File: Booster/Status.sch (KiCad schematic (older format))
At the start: 32 parts

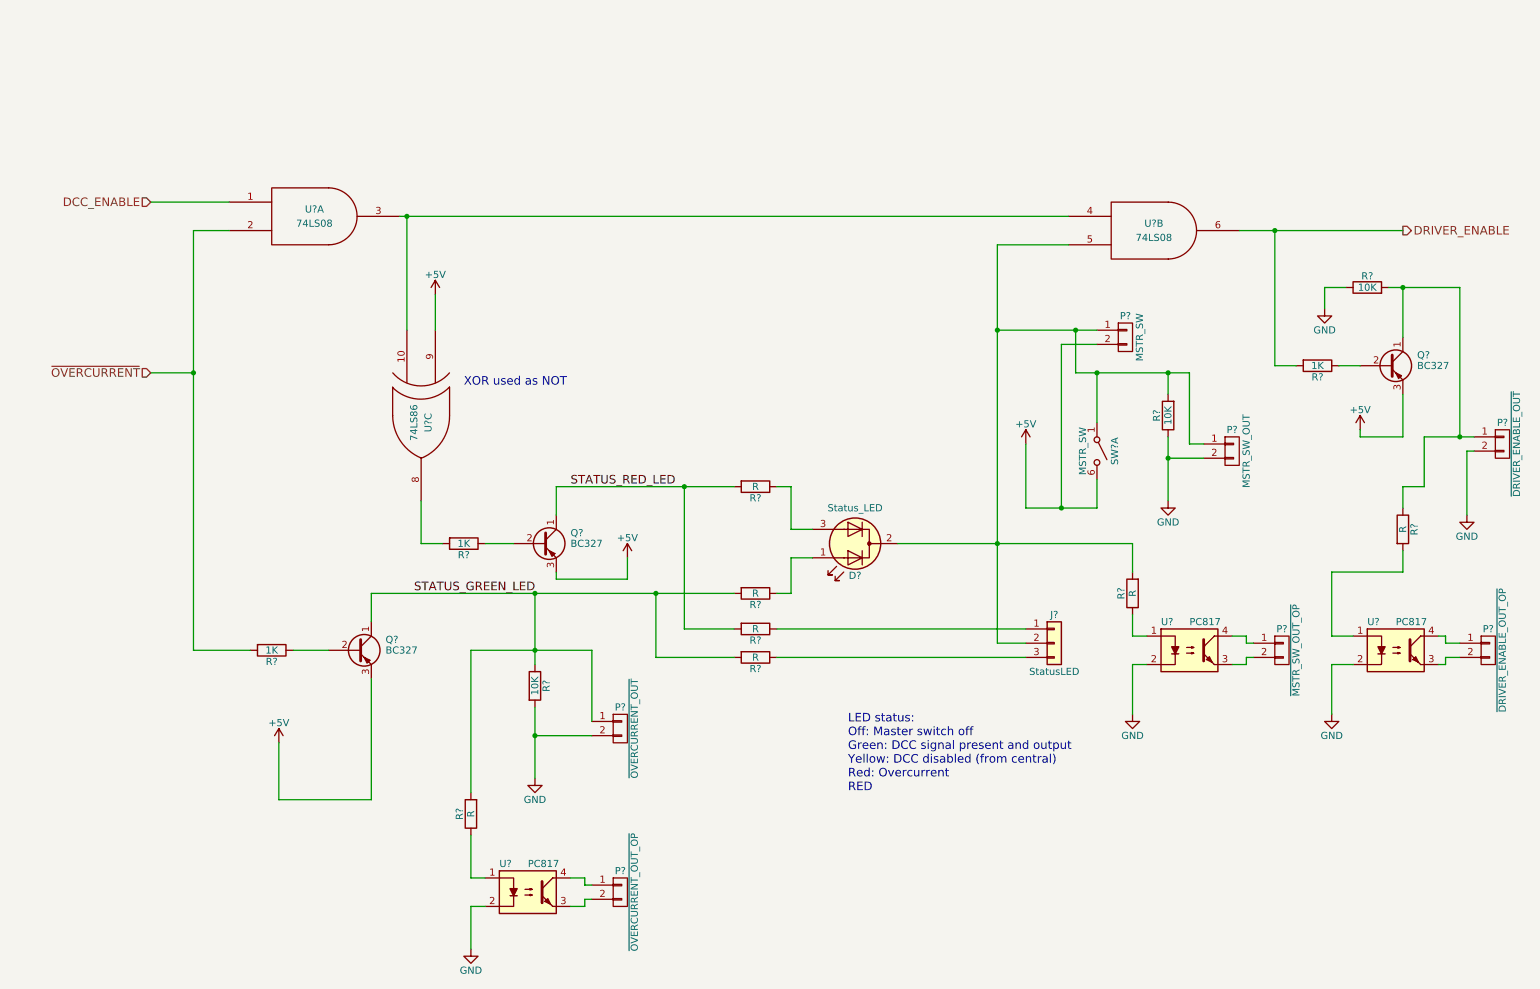
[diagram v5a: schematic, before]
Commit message: Added DCC Enable inverter. Primarely to allow meassuring track voltage easily - by enabling output with no DCC signal giving a steady 12V on the track. Replaced AND gates with NAND to free up the necessary XOR gate.
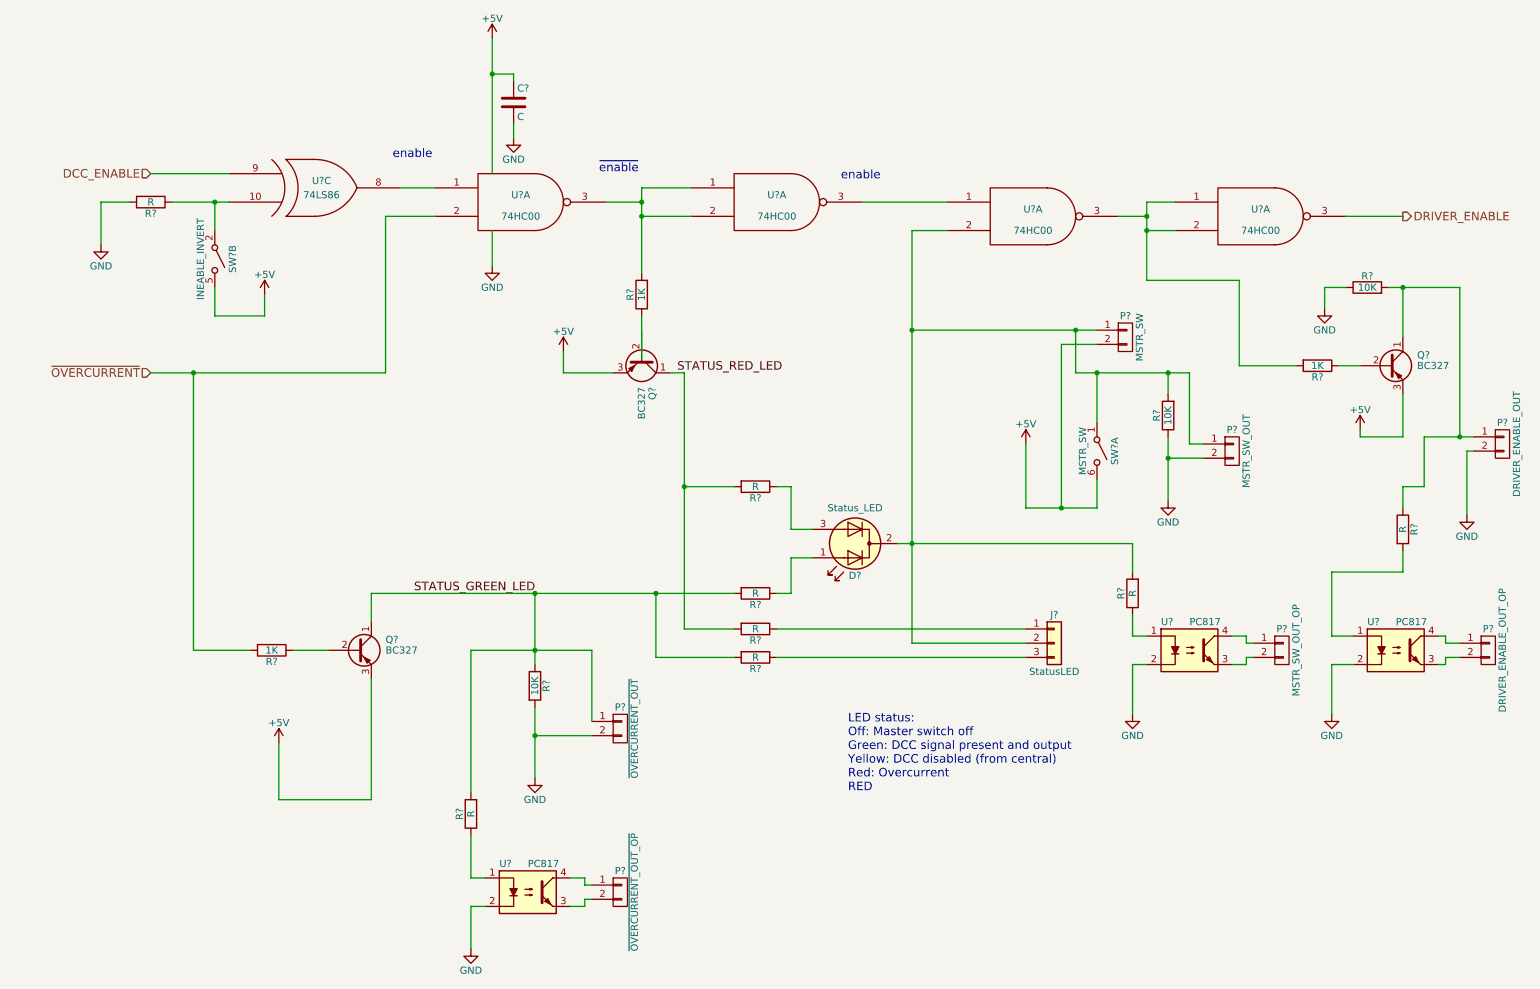
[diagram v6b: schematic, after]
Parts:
- removed U? (x2): 74LS08, symbol 74LS08
- added C?: C, symbol C
- added R?: R, symbol R
- added SW?: INEABLE_INVERT, symbol SW_SPST_x03
- added U? (x4): 74HC00, symbol 74HC00
- P?: value ~DRIVER_ENABLE_OUT -> DRIVER_ENABLE_OUT
- P?: value ~DRIVER_ENABLE_OUT_OP -> DRIVER_ENABLE_OUT_OP
- P?: value ~MSTR_SW_OUT_OP -> MSTR_SW_OUT_OP
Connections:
- net VCC is gone; now on net +5V: U?.14 (VCC)
- net +5V: now also C?.1, SW?.5 (B), U?.14 (VCC), U?.14 (VCC), U?.14 (VCC), U?.14 (VCC); no longer U?.9 (IN1)
- net DCC_ENABLE: now also U?.9 (IN1)
- net DRIVER_ENABLE: now also U?.3; no longer R?.2
- net GND: now also C?.2, R?.2, U?.7 (GND), U?.7 (GND), U?.7 (GND), U?.7 (GND)
- net ~OVERCURRENT: now also U?.2
- net at D?.2 (K), J?.2 (Pin_2), P?.1 (P1)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: now also U?.2
- net at U?.10 (IN2): now also R?.1, SW?.2 (A)
- net at R?.1: no longer Q?.2 (B)
- net at R?.2: now also U?.1, U?.2, U?.3; no longer U?.8 (OUT)
- new net: R?.2, U?.1, U?.2, U?.3
- new net: U?.1, U?.8 (OUT)
- new net: U?.1, U?.3
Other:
- note added: "enable"
- note added: "~enable"
- note removed: "XOR used as NOT"
- moved on the sheet: Q?, R?, U?C

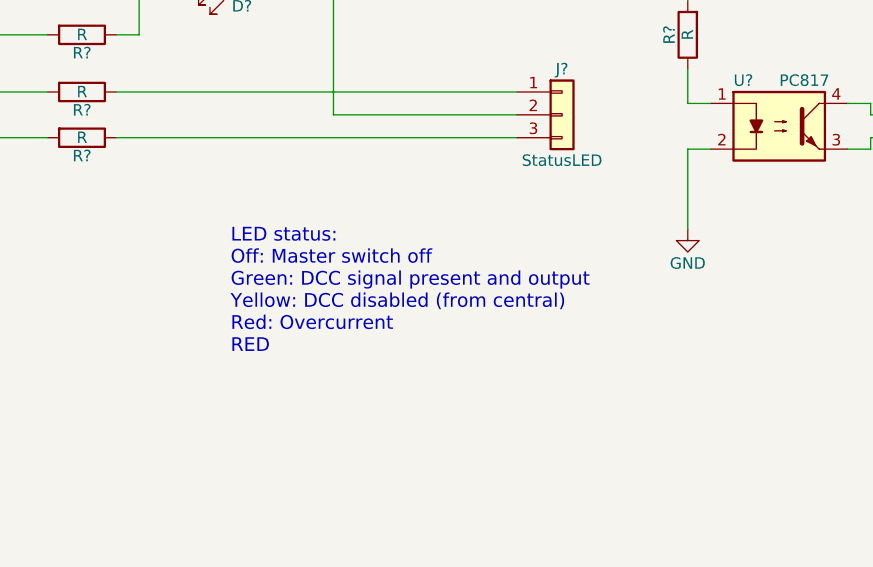
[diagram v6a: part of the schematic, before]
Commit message: Removed redundant work in text node.
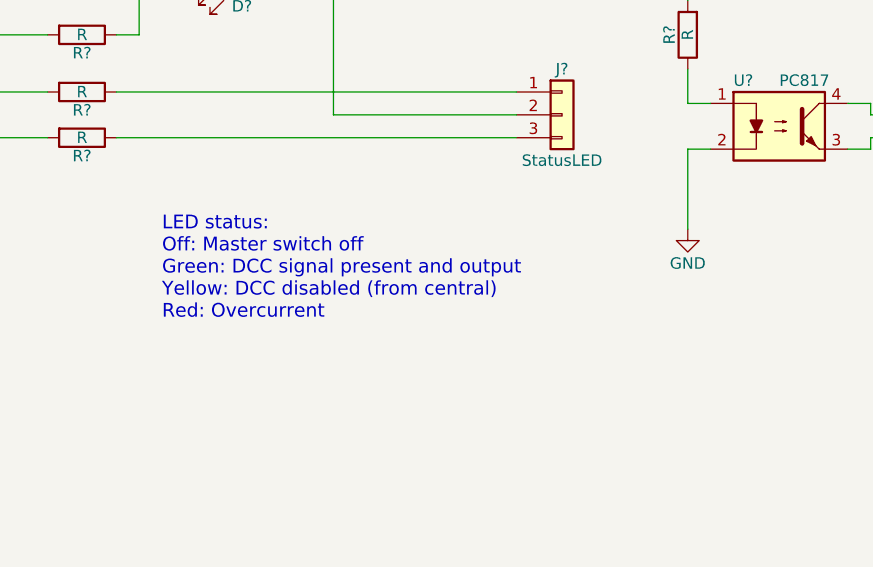
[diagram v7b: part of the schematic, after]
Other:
- note added: "LED status:\nOff: Master switch off\nGreen: DCC signal present and output\nYellow: DCC disabled (from central)\nRed: Overcurrent"
- note removed: "LED status:\nOff: Master switch off\nGreen: DCC signal present and output\nYellow: DCC disabled (from central)\nRed: Overcurrent\nRED"
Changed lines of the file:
@@
 Text HLabel 10250 2050 2    60   Output ~ 0
 DRIVER_ENABLE
-Text Notes 6350 6100 0    60   ~ 0
-LED status:\nOff: Master switch off\nGreen: DCC signal present and output\nYellow: DCC disabled (from central)\nRed: Overcurrent\nRED
+Text Notes 6050 5950 0    60   ~ 0
+LED status:\nOff: Master switch off\nGreen: DCC signal present and output\nYellow: DCC disabled (from central)\nRed: Overcurrent
 $Comp
 L LED_Dual_ACA D?

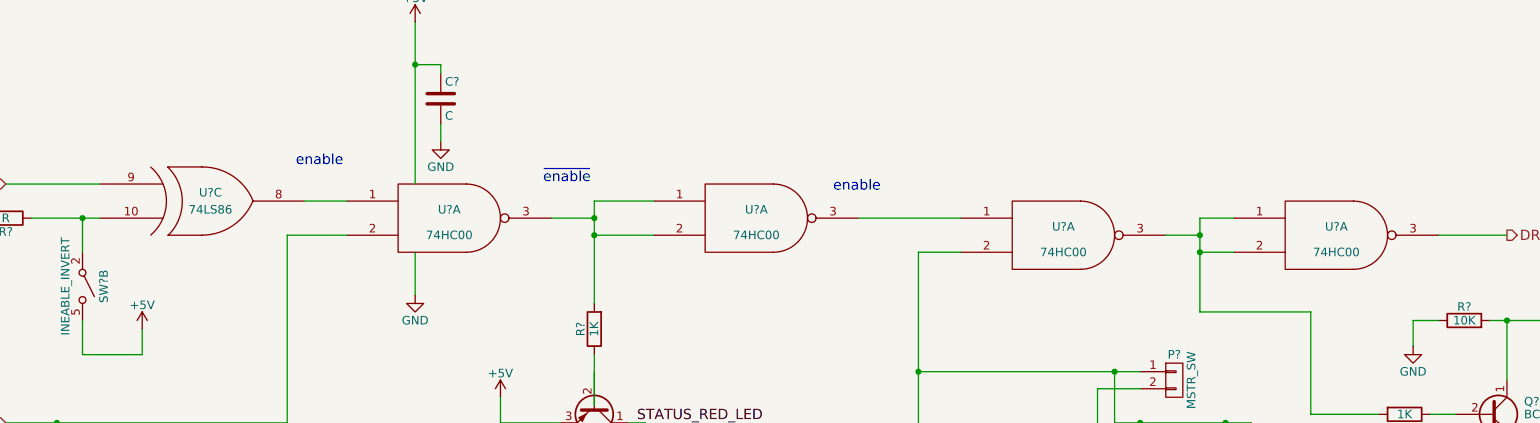
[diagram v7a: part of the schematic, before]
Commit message: Use actual test point instead of 1 pin jumpers.
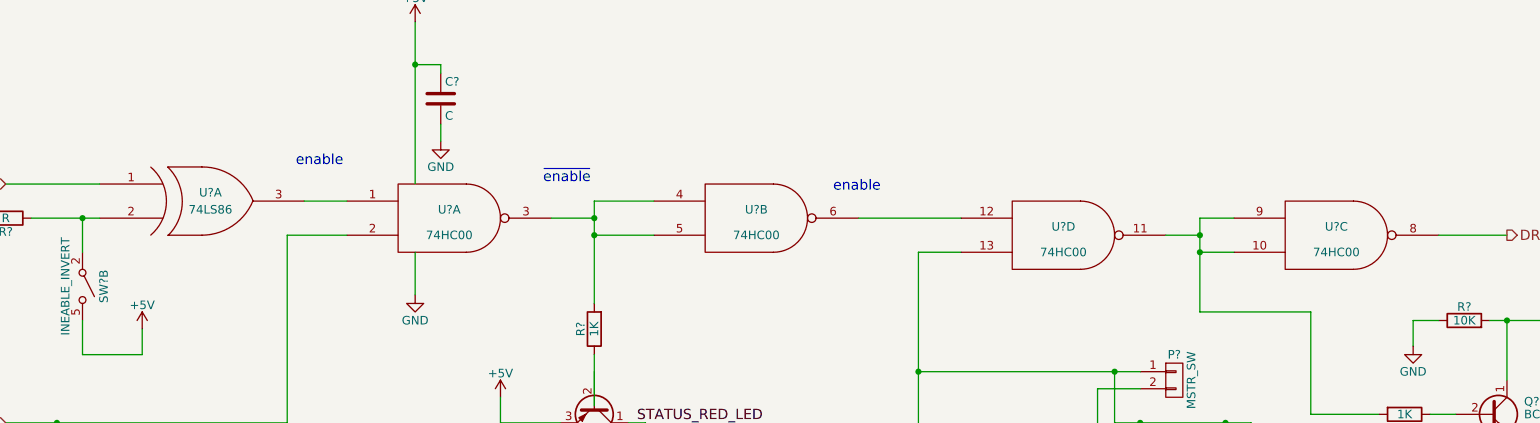
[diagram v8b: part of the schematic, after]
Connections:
- net DCC_ENABLE: now also U?.1 (IN1); no longer U?.9 (IN1)
- net DRIVER_ENABLE: now also U?.8; no longer U?.3
- net at D?.2 (K), J?.2 (Pin_2), P?.1 (P1)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: now also U?.13; no longer U?.2
- net at R?.2, U?.3: now also U?.4, U?.5; no longer U?.1, U?.2
- net at R?.1, SW?.2 (A): now also U?.2 (IN2); no longer U?.10 (IN2)
- net at U?.1: now also U?.3 (OUT); no longer U?.8 (OUT)
- new net: R?.2, U?.10, U?.11, U?.9
- new net: U?.12, U?.6
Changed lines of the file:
@@
 $Comp
 L 74LS86 U?
-U 3 1 5A0F5EBC
+U 1 1 5A0F5EBC
 P 2600 1850
 F 0 "U?" H 2650 1900 50  0000 C CNN
@@
 F 2 "" H 2600 1850 50  0001 C CNN
 F 3 "" H 2600 1850 50  0001 C CNN
-	3    2600 1850
+	1    2600 1850
 	1    0    0    -1
 $EndComp
@@
 $Comp
 L 74HC00 U?
-U 1 1 5A11F087
+U 2 1 5A11F087
 P 5850 1950
 F 0 "U?" H 5850 2000 50  0000 C CNN
@@
 F 2 "" H 5850 1950 50  0001 C CNN
 F 3 "" H 5850 1950 50  0001 C CNN
-	1    5850 1950
+	2    5850 1950
 	1    0    0    -1
 $EndComp
@@
 $Comp
 L 74HC00 U?
-U 1 1 5A1330DE
+U 4 1 5A1330DE
 P 7650 2050
 F 0 "U?" H 7650 2100 50  0000 C CNN
@@
 F 2 "" H 7650 2050 50  0001 C CNN
 F 3 "" H 7650 2050 50  0001 C CNN
-	1    7650 2050
+	4    7650 2050
 	1    0    0    -1
 $EndComp
 $Comp
 L 74HC00 U?
-U 1 1 5A13319F
+U 3 1 5A13319F
 P 9250 2050
 F 0 "U?" H 9250 2100 50  0000 C CNN
@@
 F 2 "" H 9250 2050 50  0001 C CNN
 F 3 "" H 9250 2050 50  0001 C CNN
-	1    9250 2050
+	3    9250 2050
 	1    0    0    -1
 $EndComp
